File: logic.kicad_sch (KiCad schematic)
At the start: 68 parts, among them J5 HanRun_HR911105A, Q24 2N7002, Q25 AO3401A, SW2 SW_Push, U10 LAN8720A, U11 74HC595, U17 N066-6448TSWEG03-H28, U8 SY8120B1ABC, U9 ESP32-WROOM-32E

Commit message: Finish initial layout
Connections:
- net DC_OUT1_OFF: now also U11.6 (QG); no longer U11.3 (QD)
- net DC_OUT2_OFF: now also U11.5 (QF); no longer U11.4 (QE)
- net DC_OUT3_OFF: now also U11.1 (QB); no longer U11.5 (QF)
- net DC_OUT_OFF: now also U11.3 (QD); no longer U11.15 (QA)
- net USB_OUT_OFF: now also U11.4 (QE); no longer U11.1 (QB)

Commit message: Add debouncing capacitor to front panel button
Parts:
- added C105: 22nF, Capacitor_SMD:C_0402_1005Metric, symbol Device:C_Small
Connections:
- net BUTTON: now also C105.1
- net GND: now also C105.2
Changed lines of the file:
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@@
   (junction (at 73.66 34.29) (diameter 0) (color 0 0 0 0)
+  )
+  (junction (at 194.31 44.45) (diameter 0) (color 0 0 0 0)
   )
   (junction (at 135.89 87.63) (diameter 0) (color 0 0 0 0)
@@
     (stroke (width 0) (type default) (color 0 0 0 0))
   )
+  (wire (pts (xy 194.31 44.45) (xy 195.58 44.45))
+    (stroke (width 0) (type default) (color 0 0 0 0))
+  )
   (wire (pts (xy 88.9 135.89) (xy 118.11 135.89))
     (stroke (width 0) (type default) (color 0 0 0 0))
@@
     (stroke (width 0) (type default) (color 0 0 0 0))
   )
+  (wire (pts (xy 194.31 50.8) (xy 194.31 52.07))
+    (stroke (width 0) (type default) (color 0 0 0 0))
+  )
   (wire (pts (xy 255.27 34.29) (xy 255.27 45.72))
     (stroke (width 0) (type default) (color 0 0 0 0))
@@
     (stroke (width 0) (type default) (color 0 0 0 0))
   )
-  (wire (pts (xy 187.96 44.45) (xy 195.58 44.45))
+  (wire (pts (xy 187.96 44.45) (xy 194.31 44.45))
     (stroke (width 0) (type default) (color 0 0 0 0))
   )
@@
   )
   (wire (pts (xy 71.12 43.18) (xy 73.66 43.18))
+    (stroke (width 0) (type default) (color 0 0 0 0))
+  )
+  (wire (pts (xy 194.31 44.45) (xy 194.31 45.72))
     (stroke (width 0) (type default) (color 0 0 0 0))
   )
@@
     )
     (pin "1")
+  )
+  (symbol (lib_id "Device:C_Small") (at 194.31 48.26 0) (mirror y) (unit 1)
+    (in_bom yes) (on_board yes)
+    (property "Reference" "C105" (id 0) (at 196.85 49.53 90)
+      (effects (font (size 1.27 1.27)) (justify left))
+    )
+    (property "Value" "22nF" (id 1) (at 190.5 52.07 90)
+      (effects (font (size 1.27 1.27)) (justify left))
+    )
+    (property "Footprint" "Capacitor_SMD:C_0402_1005Metric" (id 2) (at 194.31 48.26 0)
+      (effects (font (size 1.27 1.27)) hide)
+    )
+    (property "Datasheet" "~" (id 3) (at 194.31 48.26 0)
+      (effects (font (size 1.27 1.27)) hide)
+    )
+    (property "LCSC" "C1532" (id 4) (at 194.31 48.26 0)
+      (effects (font (size 1.27 1.27)) hide)
+    )
+    (pin "1")
+    (pin "2")
   )
   (symbol (lib_id "power:GND") (at 53.34 58.42 0) (unit 1)
@@
     (pin "2")
   )
+  (symbol (lib_id "power:GND") (at 194.31 52.07 0) (unit 1)
+    (in_bom yes) (on_board yes) (fields_autoplaced)
+    (property "Reference" "#PWR0307" (id 0) (at 194.31 58.42 0)
+      (effects (font (size 1.27 1.27)) hide)
+    )
+    (property "Value" "GND" (id 1) (at 194.31 56.5134 0))
+    (property "Footprint" "" (id 2) (at 194.31 52.07 0)
+      (effects (font (size 1.27 1.27)) hide)
+    )
+    (property "Datasheet" "" (id 3) (at 194.31 52.07 0)
+      (effects (font (size 1.27 1.27)) hide)
+    )
+    (pin "1")
+  )
   (symbol (lib_id "power:GND") (at 161.29 124.46 0) (unit 1)

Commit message: Add SMBUS and I2C debug headers
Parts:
- added J10: I2C, Connector_PinHeader_2.54mm:PinHeader_1x04_P2.54mm_Vertical, symbol Connector_Generic:Conn_01x04
- added J4: SMBUS, Connector_PinHeader_2.54mm:PinHeader_1x04_P2.54mm_Vertical, symbol Connector_Generic:Conn_01x04
- added R122, R123: 100R, Resistor_SMD:R_0402_1005Metric, symbol Device:R_Small
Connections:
- net +3V3: now also R122.2, R123.2
- net GND: now also J10.1 (Pin_1), J4.1 (Pin_1)
- net SCL: now also J10.2 (Pin_2)
- net SDA: now also J10.3 (Pin_3)
- net SMBC: now also J4.2 (Pin_2)
- net SMBD: now also J4.3 (Pin_3)
- new net: J4.4 (Pin_4), R122.1
- new net: J10.4 (Pin_4), R123.1

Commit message: Add more voltage rail LEDs
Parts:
- added D?: GRN, LED_SMD:LED_0603_1608Metric, symbol Device:LED_Small
- added D?: YEL, LED_SMD:LED_0603_1608Metric, symbol Device:LED_Small
- added R? (x2): 5.1k, Resistor_SMD:R_0402_1005Metric, symbol Device:R_Small
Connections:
- net +3V3: now also R?.1
- net ESP32 Debug/VBUS: now also R?.1
- net GND: now also D?.1 (K), D?.1 (K)
- new net: D?.2 (A), R?.2 (x2)
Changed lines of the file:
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@@
   (junction (at 87.63 116.84) (diameter 0) (color 0 0 0 0)
   )
+  (junction (at 73.66 57.15) (diameter 0) (color 0 0 0 0)
+  )
   (junction (at 67.31 116.84) (diameter 0) (color 0 0 0 0)
   )
@@
   (junction (at 120.65 124.46) (diameter 0) (color 0 0 0 0)
   )
+  (junction (at 132.08 34.29) (diameter 0) (color 0 0 0 0)
+  )
   (junction (at 135.89 95.25) (diameter 0) (color 0 0 0 0)
   )
@@
     (stroke (width 0) (type default) (color 0 0 0 0))
   )
+  (wire (pts (xy 85.09 57.15) (xy 73.66 57.15))
+    (stroke (width 0) (type default) (color 0 0 0 0))
+  )
   (wire (pts (xy 100.33 124.46) (xy 93.98 124.46))
     (stroke (width 0) (type default) (color 0 0 0 0))
@@
     (stroke (width 0) (type default) (color 0 0 0 0))
   )
-  (wire (pts (xy 73.66 54.61) (xy 73.66 59.69))
+  (wire (pts (xy 73.66 54.61) (xy 73.66 57.15))
     (stroke (width 0) (type default) (color 0 0 0 0))
   )
@@
     (stroke (width 0) (type default) (color 0 0 0 0))
   )
+  (wire (pts (xy 144.78 25.4) (xy 146.05 25.4))
+    (stroke (width 0) (type default) (color 0 0 0 0))
+  )
   (wire (pts (xy 88.9 135.89) (xy 88.9 134.62))
     (stroke (width 0) (type default) (color 0 0 0 0))
@@
     (stroke (width 0) (type default) (color 0 0 0 0))
   )
+  (wire (pts (xy 132.08 25.4) (xy 132.08 34.29))
+    (stroke (width 0) (type default) (color 0 0 0 0))
+  )
   (wire (pts (xy 87.63 151.13) (xy 88.9 151.13))
     (stroke (width 0) (type default) (color 0 0 0 0))
@@
     (stroke (width 0) (type default) (color 0 0 0 0))
   )
+  (wire (pts (xy 146.05 25.4) (xy 146.05 26.67))
+    (stroke (width 0) (type default) (color 0 0 0 0))
+  )
   (wire (pts (xy 227.33 53.34) (xy 245.11 53.34))
     (stroke (width 0) (type default) (color 0 0 0 0))
@@
     (stroke (width 0) (type default) (color 0 0 0 0))
   )
+  (wire (pts (xy 132.08 34.29) (xy 137.16 34.29))
+    (stroke (width 0) (type default) (color 0 0 0 0))
+  )
   (wire (pts (xy 146.05 41.91) (xy 146.05 40.64))
     (stroke (width 0) (type default) (color 0 0 0 0))
@@
     (stroke (width 0) (type default) (color 0 0 0 0))
   )
+  (wire (pts (xy 85.09 64.77) (xy 85.09 66.04))
+    (stroke (width 0) (type default) (color 0 0 0 0))
+  )
   (wire (pts (xy 158.75 40.64) (xy 160.02 40.64))
     (stroke (width 0) (type default) (color 0 0 0 0))
@@
     (stroke (width 0) (type default) (color 0 0 0 0))
   )
+  (wire (pts (xy 73.66 57.15) (xy 73.66 59.69))
+    (stroke (width 0) (type default) (color 0 0 0 0))
+  )
   (wire (pts (xy 266.7 86.36) (xy 266.7 85.09))
     (stroke (width 0) (type default) (color 0 0 0 0))
@@
     (stroke (width 0) (type default) (color 0 0 0 0))
   )
+  (wire (pts (xy 85.09 59.69) (xy 85.09 57.15))
+    (stroke (width 0) (type default) (color 0 0 0 0))
+  )
   (wire (pts (xy 227.33 76.2) (xy 256.54 76.2))
     (stroke (width 0) (type default) (color 0 0 0 0))
@@
     (stroke (width 0) (type default) (color 0 0 0 0))
   )
+  (wire (pts (xy 133.35 25.4) (xy 132.08 25.4))
+    (stroke (width 0) (type default) (color 0 0 0 0))
+  )
   (wire (pts (xy 87.63 135.89) (xy 88.9 135.89))
     (stroke (width 0) (type default) (color 0 0 0 0))
@@
     (stroke (width 0) (type default) (color 0 0 0 0))
   )
+  (wire (pts (xy 85.09 71.12) (xy 85.09 72.39))
+    (stroke (width 0) (type default) (color 0 0 0 0))
+  )
   (wire (pts (xy 73.66 107.95) (xy 72.39 107.95))
     (stroke (width 0) (type default) (color 0 0 0 0))
@@
     (stroke (width 0) (type default) (color 0 0 0 0))
   )
+  (wire (pts (xy 138.43 25.4) (xy 139.7 25.4))
+    (stroke (width 0) (type default) (color 0 0 0 0))
+  )
   (wire (pts (xy 69.85 176.53) (xy 69.85 177.8))
     (stroke (width 0) (type default) (color 0 0 0 0))
@@
     (stroke (width 0) (type default) (color 0 0 0 0))
   )
-  (wire (pts (xy 128.27 34.29) (xy 137.16 34.29))
+  (wire (pts (xy 128.27 34.29) (xy 132.08 34.29))
     (stroke (width 0) (type default) (color 0 0 0 0))
   )
@@
     (pin "2")
   )
+  (symbol (lib_id "Device:R_Small") (at 135.89 25.4 90) (mirror x) (unit 1)
+    (in_bom yes) (on_board yes) (fields_autoplaced)
+    (property "Reference" "R?" (id 0) (at 135.89 20.9636 90))
+    (property "Value" "5.1k" (id 1) (at 135.89 23.5005 90))
+    (property "Footprint" "Resistor_SMD:R_0402_1005Metric" (id 2) (at 135.89 25.4 0)
+      (effects (font (size 1.27 1.27)) hide)
+    )
+    (property "Datasheet" "~" (id 3) (at 135.89 25.4 0)
+      (effects (font (size 1.27 1.27)) hide)
+    )
+    (property "LCSC" "C25905" (id 4) (at 135.89 25.4 0)
+      (effects (font (size 1.27 1.27)) hide)
+    )
+    (pin "1")
+    (pin "2")
+  )
   (symbol (lib_id "Device:C_Small") (at 208.28 27.94 90) (unit 1)
     (in_bom yes) (on_board yes) (fields_autoplaced)
@@
     (pin "2")
   )
+  (symbol (lib_id "Device:LED_Small") (at 85.09 68.58 270) (mirror x) (unit 1)
+    (in_bom yes) (on_board yes) (fields_autoplaced)
+    (property "Reference" "D?" (id 0) (at 87.503 67.6818 90)
+      (effects (font (size 1.27 1.27)) (justify left))
+    )
+    (property "Value" "GRN" (id 1) (at 87.503 70.2187 90)
+      (effects (font (size 1.27 1.27)) (justify left))
+    )
+    (property "Footprint" "LED_SMD:LED_0603_1608Metric" (id 2) (at 85.09 68.58 90)
+      (effects (font (size 1.27 1.27)) hide)
+    )
+    (property "Datasheet" "~" (id 3) (at 85.09 68.58 90)
+      (effects (font (size 1.27 1.27)) hide)
+    )
+    (property "LCSC" "C72043" (id 4) (at 85.09 68.58 0)
+      (effects (font (size 1.27 1.27)) hide)
+    )
+    (pin "1")
+    (pin "2")
+  )
+  (symbol (lib_id "power:GND") (at 85.09 72.39 0) (unit 1)
+    (in_bom yes) (on_board yes) (fields_autoplaced)
+    (property "Reference" "#PWR?" (id 0) (at 85.09 78.74 0)
+      (effects (font (size 1.27 1.27)) hide)
+    )
+    (property "Value" "GND" (id 1) (at 85.09 76.8334 0))
+    (property "Footprint" "" (id 2) (at 85.09 72.39 0)
+      (effects (font (size 1.27 1.27)) hide)
+    )
+    (property "Datasheet" "" (id 3) (at 85.09 72.39 0)
+      (effects (font (size 1.27 1.27)) hide)
+    )
+    (pin "1")
+  )
   (symbol (lib_id "power:+3V3") (at 69.85 97.79 0) (unit 1)
     (in_bom yes) (on_board yes) (fields_autoplaced)
@@
     (pin "1")
   )
+  (symbol (lib_id "Device:LED_Small") (at 142.24 25.4 180) (unit 1)
+    (in_bom yes) (on_board yes) (fields_autoplaced)
+    (property "Reference" "D?" (id 0) (at 142.1765 20.6842 0))
+    (property "Value" "YEL" (id 1) (at 142.1765 23.2211 0))
+    (property "Footprint" "LED_SMD:LED_0603_1608Metric" (id 2) (at 142.24 25.4 90)
+      (effects (font (size 1.27 1.27)) hide)
+    )
+    (property "Datasheet" "~" (id 3) (at 142.24 25.4 90)
+      (effects (font (size 1.27 1.27)) hide)
+    )
+    (property "LCSC" "C72038" (id 4) (at 142.24 25.4 0)
+      (effects (font (size 1.27 1.27)) hide)
+    )
+    (pin "1")
+    (pin "2")
+  )
   (symbol (lib_id "Device:R_Small") (at 105.41 128.27 0) (unit 1)
     (in_bom yes) (on_board yes) (fields_autoplaced)
@@
     (pin "1")
   )
+  (symbol (lib_id "Device:R_Small") (at 85.09 62.23 0) (mirror y) (unit 1)
+    (in_bom yes) (on_board yes) (fields_autoplaced)
+    (property "Reference" "R?" (id 0) (at 86.5886 61.3953 0)
+      (effects (font (size 1.27 1.27)) (justify right))
+    )
+    (property "Value" "5.1k" (id 1) (at 86.5886 63.9322 0)
+      (effects (font (size 1.27 1.27)) (justify right))
+    )
+    (property "Footprint" "Resistor_SMD:R_0402_1005Metric" (id 2) (at 85.09 62.23 0)
+      (effects (font (size 1.27 1.27)) hide)
+    )
+    (property "Datasheet" "~" (id 3) (at 85.09 62.23 0)
+      (effects (font (size 1.27 1.27)) hide)
+    )
+    (property "LCSC" "C25905" (id 4) (at 85.09 62.23 0)
+      (effects (font (size 1.27 1.27)) hide)
+    )
+    (pin "1")
+    (pin "2")
+  )
   (symbol (lib_id "Device:R_Small") (at 185.42 29.21 0) (unit 1)
     (in_bom yes) (on_board yes) (fields_autoplaced)
@@
     (pin "2")
   )
+  (symbol (lib_id "power:GND") (at 146.05 26.67 0) (unit 1)
+    (in_bom yes) (on_board yes) (fields_autoplaced)
+    (property "Reference" "#PWR?" (id 0) (at 146.05 33.02 0)
+      (effects (font (size 1.27 1.27)) hide)
+    )
+    (property "Value" "GND" (id 1) (at 146.05 31.1134 0))
+    (property "Footprint" "" (id 2) (at 146.05 26.67 0)
+      (effects (font (size 1.27 1.27)) hide)
+    )
+    (property "Datasheet" "" (id 3) (at 146.05 26.67 0)
+      (effects (font (size 1.27 1.27)) hide)
+    )
+    (pin "1")
+  )
   (symbol (lib_id "power:+3V3") (at 41.91 118.11 0) (unit 1)

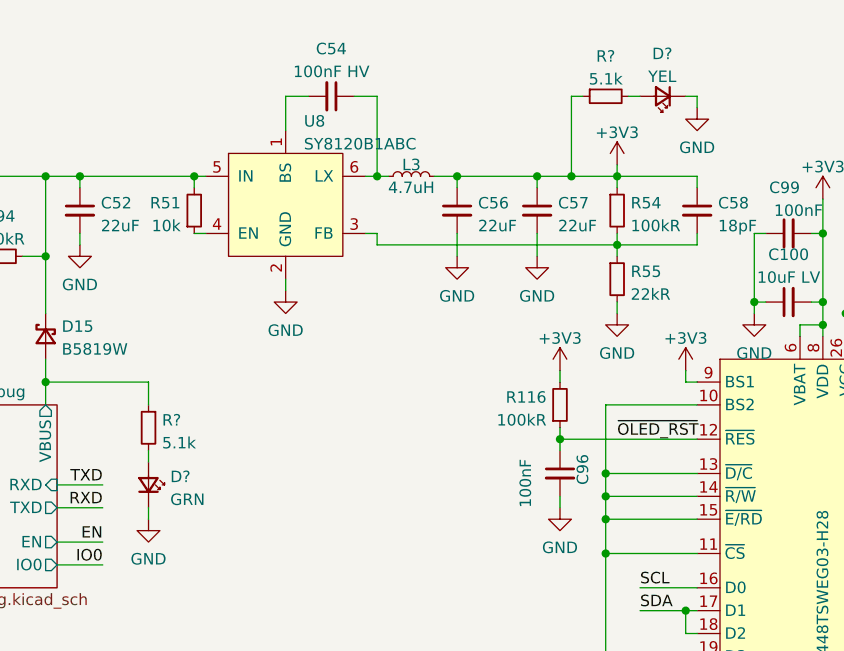
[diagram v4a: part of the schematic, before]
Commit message: Fix footprint origins for JLC assembly
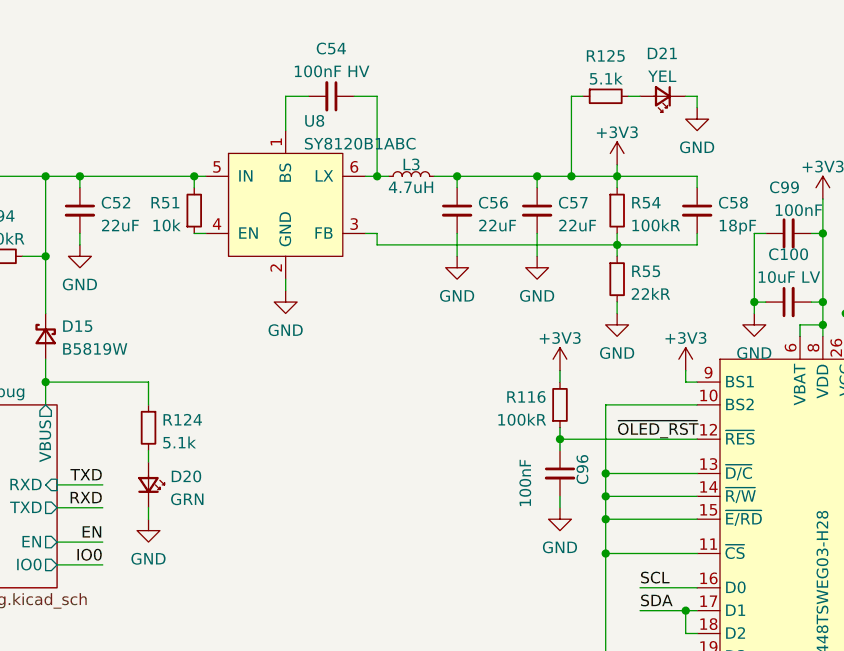
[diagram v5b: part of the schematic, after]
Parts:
- C52, C55, C56, C57: LCSC C45783 -> C602037
- J10, J4: now left out of the parts list
- U10: LCSC (none) -> C45223
- gave numbers to parts that had none: 4
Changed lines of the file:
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@@
   )
   (symbol (lib_id "Connector_Generic:Conn_01x04") (at 105.41 180.34 180) (unit 1)
-    (in_bom yes) (on_board yes) (fields_autoplaced)
+    (in_bom no) (on_board yes) (fields_autoplaced)
     (property "Reference" "J4" (id 0) (at 105.41 170.2902 0))
     (property "Value" "SMBUS" (id 1) (at 105.41 172.8271 0))
@@
     )
     (property "Datasheet" "http://ww1.microchip.com/downloads/en/DeviceDoc/8720a.pdf" (id 3) (at 64.77 172.72 0)
+      (effects (font (size 1.27 1.27)) hide)
+    )
+    (property "LCSC" "C45223" (id 4) (at 69.85 148.59 0)
       (effects (font (size 1.27 1.27)) hide)
     )
@@
       (effects (font (size 1.27 1.27)) hide)
     )
-    (property "LCSC" "C45783" (id 4) (at 128.27 38.1 0)
+    (property "LCSC" "C602037" (id 4) (at 128.27 38.1 0)
       (effects (font (size 1.27 1.27)) hide)
     )
@@
   (symbol (lib_id "Device:R_Small") (at 135.89 25.4 90) (mirror x) (unit 1)
     (in_bom yes) (on_board yes) (fields_autoplaced)
-    (property "Reference" "R?" (id 0) (at 135.89 20.9636 90))
+    (property "Reference" "R125" (id 0) (at 135.89 20.9636 90))
     (property "Value" "5.1k" (id 1) (at 135.89 23.5005 90))
     (property "Footprint" "Resistor_SMD:R_0402_1005Metric" (id 2) (at 135.89 25.4 0)
@@
       (effects (font (size 1.27 1.27)) hide)
     )
-    (property "LCSC" "C45783" (id 4) (at 208.28 27.94 0)
+    (property "LCSC" "C602037" (id 4) (at 208.28 27.94 0)
       (effects (font (size 1.27 1.27)) hide)
     )
@@
   (symbol (lib_id "Device:LED_Small") (at 85.09 68.58 270) (mirror x) (unit 1)
     (in_bom yes) (on_board yes) (fields_autoplaced)
-    (property "Reference" "D?" (id 0) (at 87.503 67.6818 90)
+    (property "Reference" "D20" (id 0) (at 87.503 67.6818 90)
       (effects (font (size 1.27 1.27)) (justify left))
     )
@@
   (symbol (lib_id "power:GND") (at 85.09 72.39 0) (unit 1)
     (in_bom yes) (on_board yes) (fields_autoplaced)
-    (property "Reference" "#PWR?" (id 0) (at 85.09 78.74 0)
+    (property "Reference" "#PWR0313" (id 0) (at 85.09 78.74 0)
       (effects (font (size 1.27 1.27)) hide)
     )
@@
       (effects (font (size 1.27 1.27)) hide)
     )
-    (property "LCSC" "C45783" (id 4) (at 77.47 38.1 0)
+    (property "LCSC" "C602037" (id 4) (at 77.47 38.1 0)
       (effects (font (size 1.27 1.27)) hide)
     )
@@
       (effects (font (size 1.27 1.27)) hide)
     )
-    (property "LCSC" "C45783" (id 4) (at 119.38 38.1 0)
+    (property "LCSC" "C602037" (id 4) (at 119.38 38.1 0)
       (effects (font (size 1.27 1.27)) hide)
     )
@@
   (symbol (lib_id "Device:LED_Small") (at 142.24 25.4 180) (unit 1)
     (in_bom yes) (on_board yes) (fields_autoplaced)
-    (property "Reference" "D?" (id 0) (at 142.1765 20.6842 0))
+    (property "Reference" "D21" (id 0) (at 142.1765 20.6842 0))
     (property "Value" "YEL" (id 1) (at 142.1765 23.2211 0))
     (property "Footprint" "LED_SMD:LED_0603_1608Metric" (id 2) (at 142.24 25.4 90)
@@
   (symbol (lib_id "Device:R_Small") (at 85.09 62.23 0) (mirror y) (unit 1)
     (in_bom yes) (on_board yes) (fields_autoplaced)
-    (property "Reference" "R?" (id 0) (at 86.5886 61.3953 0)
+    (property "Reference" "R124" (id 0) (at 86.5886 61.3953 0)
       (effects (font (size 1.27 1.27)) (justify right))
     )
@@
   (symbol (lib_id "power:GND") (at 146.05 26.67 0) (unit 1)
     (in_bom yes) (on_board yes) (fields_autoplaced)
-    (property "Reference" "#PWR?" (id 0) (at 146.05 33.02 0)
+    (property "Reference" "#PWR0312" (id 0) (at 146.05 33.02 0)
       (effects (font (size 1.27 1.27)) hide)
     )
@@
   )
   (symbol (lib_id "Connector_Generic:Conn_01x04") (at 125.73 179.07 180) (unit 1)
-    (in_bom yes) (on_board yes) (fields_autoplaced)
+    (in_bom no) (on_board yes) (fields_autoplaced)
     (property "Reference" "J10" (id 0) (at 125.73 169.0202 0))
     (property "Value" "I2C" (id 1) (at 125.73 171.5571 0))
